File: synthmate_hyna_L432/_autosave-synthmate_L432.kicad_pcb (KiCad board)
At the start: 4 copper layers, 74 x 23 mm, 43 parts, among them J1 USB_C_synthmate, J3 USB_C_connector_board, J5 Conn_01x15, J7 Conn_01x04, J8 Conn_ST_STDC14, SW1 RotaryEncoder_Switch, SW2 SW_Push, SW3 SW_Push, U1 STM32L432KCUx, U2 TS3USB221ARSER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

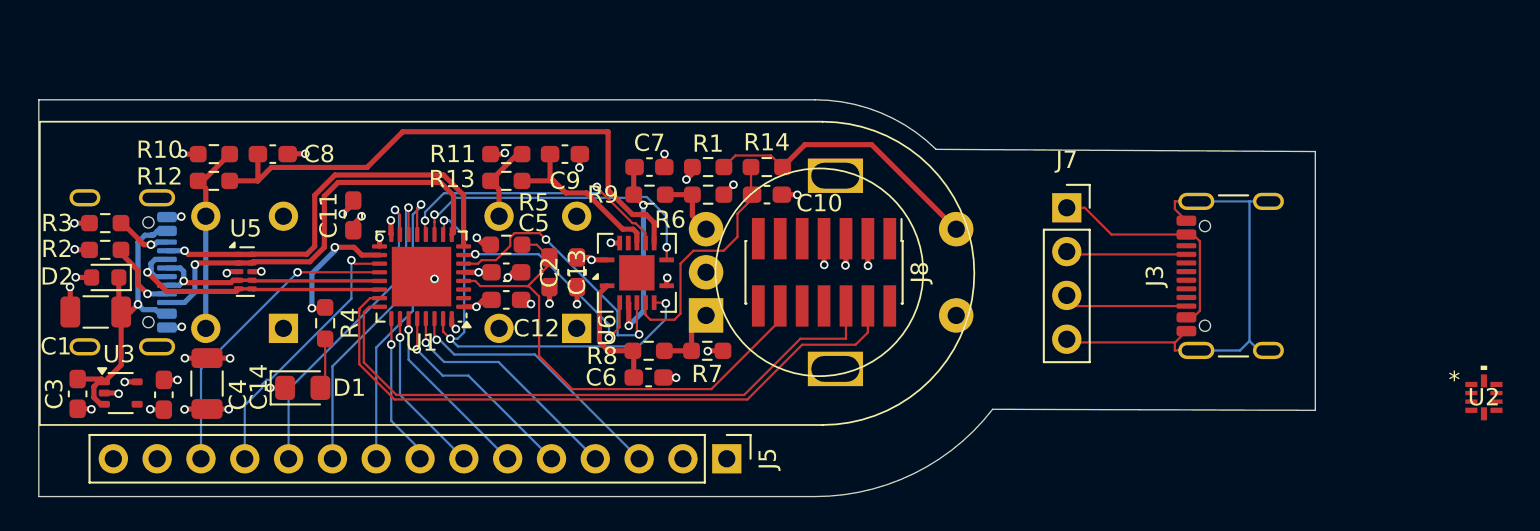
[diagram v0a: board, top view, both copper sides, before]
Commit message: added analog mux on main board nd adapter board
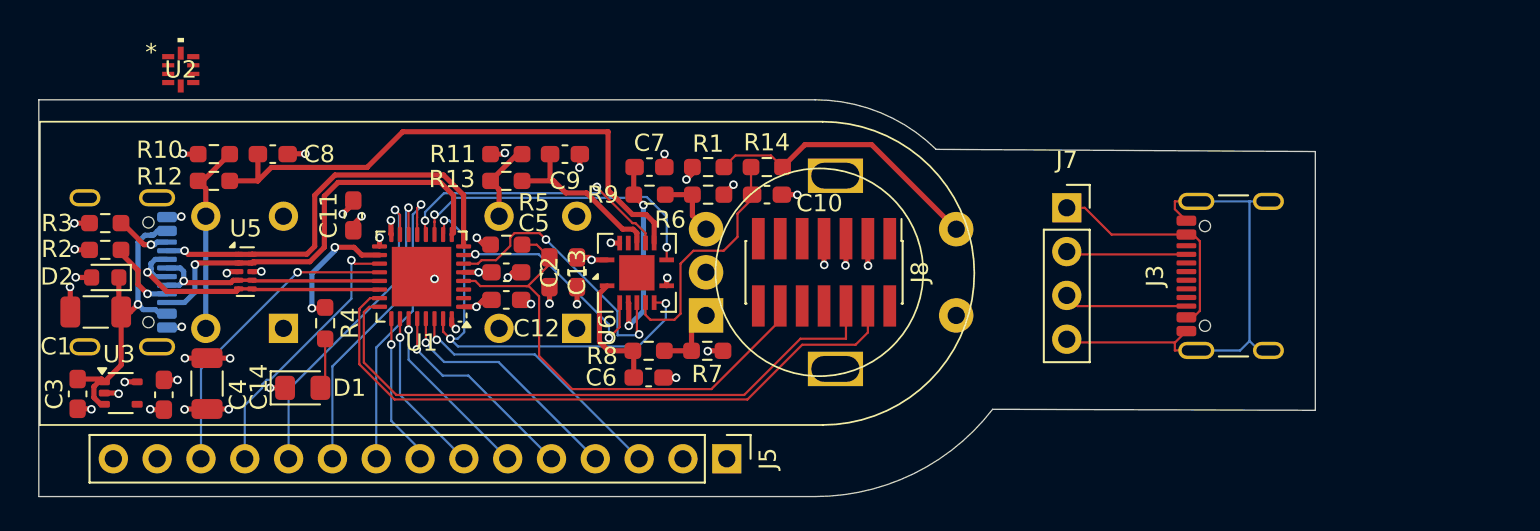
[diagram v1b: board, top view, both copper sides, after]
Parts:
- moved U2 77.9 mm to (99.2, 35.2)
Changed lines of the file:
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@@
 	(footprint "footprints:RSE10"
 		(layer "F.Cu")
-		(at 174.7726 54.249999)
+		(at 99.2274 35.25)
 		(tags "TS3USB221ARSER ")
 		(property "Reference" "U2"
